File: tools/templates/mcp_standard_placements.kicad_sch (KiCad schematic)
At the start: 150 parts, among them J1 ICSP, J3 PIR BOARD, J5 MOTOR, J6 DNP, Q1 FMOS3401A?, Q11 MMBTA55?, Q2 BC847B?, Q3 MMBTA55?, Q4 MMBTA55?, Q5 MMBTA55?, Q6 MMBTA55?, Q7 BC857C?, Q8 N/P pair? (372A), Q9 DNP, U1 S-1200B45? [pins], U106 U6A / DNP, U2 SN74LVC2G14DBV?, U3 SGM8542XS, U4 PIC16F18855, U5 MX512H, U6 S-812C33AMC? / 3.3V, U7 DNP, Y1 20 MHz

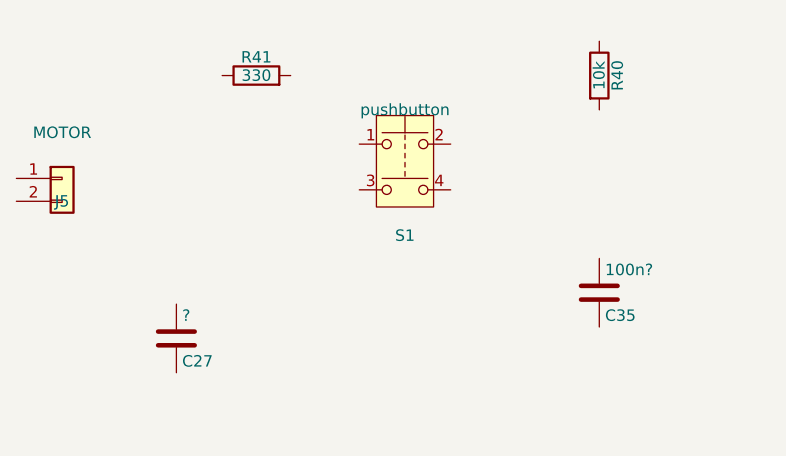
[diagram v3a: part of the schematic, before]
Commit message: Assign stock S1 tactile footprint from measured body dimensions
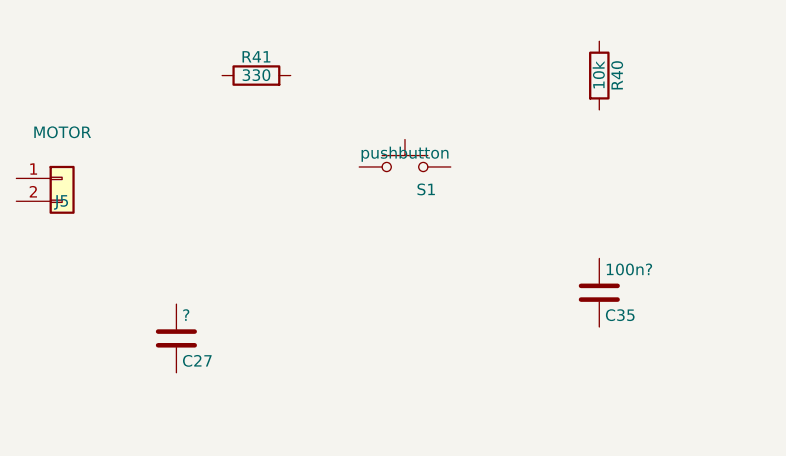
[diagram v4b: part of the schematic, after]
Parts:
- removed S1: pushbutton, symbol Switch:SW_Push_Dual
- added S1: pushbutton, Button_Switch_SMD:SW_SPST_PTS645Sx43SMTR92, symbol Switch:SW_Push
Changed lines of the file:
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@@
 	)
 	(symbol
-		(lib_id "Switch:SW_Push_Dual")
-		(at 537.21 60.96 0)
-		(unit 1)
-		(body_style 1)
-		(exclude_from_sim no)
-		(in_bom yes)
-		(on_board yes)
-		(in_pos_files yes)
-		(dnp no)
-		(property "Reference" "S1"
-			(at 537.21 68.58 0)
-			(show_name no)
-			(do_not_autoplace no)
-			(effects
-				(font
-					(size 1.27 1.27)
-				)
-			)
-		)
-		(property "Value" "pushbutton"
-			(at 537.21 54.61 0)
-			(show_name no)
-			(do_not_autoplace no)
-			(effects
-				(font
-					(size 1.27 1.27)
-				)
-			)
-		)
-		(property "Footprint" ""
-			(at 537.21 68.58 0)
-			(hide yes)
-			(show_name no)
-			(do_not_autoplace no)
-			(effects
-				(font
-					(size 1.27 1.27)
-				)
-			)
-		)
-		(property "Datasheet" ""
-			(at 537.21 60.96 0)
-			(hide yes)
-			(show_name no)
-			(do_not_autoplace no)
-			(effects
-				(font
-					(size 1.27 1.27)
-				)
-			)
-		)
-		(property "Description" "Push button switch, generic, symbol, four pins"
-			(at 537.21 60.96 0)
-			(hide yes)
-			(show_name no)
-			(do_not_autoplace no)
-			(effects
-				(font
-					(size 1.27 1.27)
-				)
-			)
-		)
-		(property "ConnectionEvidence" "v0.9.21 user annotated S1 upper-right to C35 upper/model2 (GND via prior V018); lower-right to C35 lower/model1, R40 lower/model2 and R41 left/model2. User explicitly confirms R41 right/model1 reaches J1 VPP/MCLR. Correct physical-to-native switch mapping TL=1, TR=3, BL=2, BR=4. Top-row/bottom-row common pairs remain a tactile-switch hypothesis; released/pressed behavior has not been measured."
-			(at 537.21 60.96 0)
-			(effects
-				(font
-					(size 1.27 1.27)
-				)
-				(hide yes)
-			)
-		)
-		(pin "1"
-		)
-		(pin "2"
-		)
-		(pin "3"
-		)
-		(pin "4"
-		)
-		(instances
-			(project "PetSafe_1001339"
-				(path "/33a03d59-1679-4e9c-af69-68d086b519af"
-					(reference "S1")
-					(unit 1)
-				)
-			)
-		)
-	)
-	(symbol
 		(lib_id "Device:C")
 		(at 558.8 74.93 0)
@@
 		(at 320.03999999999996 312.42)
 	)
-	(sheet_instances
+	(symbol (lib_id "Switch:SW_Push") (at 537.21 60.96 0) (unit 1)
+(body_style 1) (exclude_from_sim no) (in_bom yes) (on_board yes) (in_pos_files yes) (dnp no)
+(property "Reference" "S1"
+(at 538.48 63.5 0)
+(show_name no)
+(do_not_autoplace no)
+(effects
+				(font
+					(size 1.27 1.27)
+				)
+				(justify left)
+			)
+)
+(property "Value" "pushbutton"
+(at 537.21 59.436 0)
+(show_name no)
+(do_not_autoplace no)
+(effects
+				(font
+					(size 1.27 1.27)
+				)
+			)
+)
+(property "Footprint" "Button_Switch_SMD:SW_SPST_PTS645Sx43SMTR92"
+(at 537.21 66.04 0)
+(hide yes)
+(show_name no)
+(do_not_autoplace no)
+(effects
+				(font
+					(size 1.27 1.27)
+				)
+			)
+)
+(property "Datasheet" "https://www.ckswitches.com/media/1471/pts645.pdf"
+(at 537.21 66.04 0)
+(hide yes)
+(show_name no)
+(do_not_autoplace no)
+(effects
+				(font
+					(size 1.27 1.27)
+				)
+			)
+)
+(property "Description" "Push button switch, generic, symbol, four pins"
+(at 537.21 60.96 0)
+(hide yes)
+(show_name no)
+(do_not_autoplace no)
+(effects
+				(font
+					(size 1.27 1.27)
+				)
+			)
+)
+(property "ConnectionEvidence" "v0.9.23 retains the v0.9.21 button circuit: upper row TL/TR -> GND/C35.2, lower row BL/BR -> H_BUTTON/C35.1/R40.2/R41.2; R41.1 -> J1 VPP. Stock Switch:SW_Push represents the two contact nodes, with physical TL/TR -> native pin1 and BL/BR -> pin2. Four physical pads remain recorded. Common pairs and released/pressed behavior remain inferred from tactile-switch construction, not newly measured." (at 537.21 60.96 0)
+(effects (font (size 1.27 1.27)) (hide yes))
+)
+(property "MechanicalEvidence" "User measured a 6 x 6 x 4 mm body plus 2 mm actuator (about 6 mm overall). Photo shows four SMD gullwing leads; approximate pad-centre span from photo/body ratio is about 8 mm, consistent with the stock PTS645 land pattern (7.96 x 4.50 mm centres). Dimensions select a candidate family, not an exact manufacturer. Library x43 footprint/3D model denotes 4.3 mm overall and must not be used as the measured 6 mm housing." (at 537.21 60.96 0)
+(effects (font (size 1.27 1.27)) (hide yes))
+)
+(property "BodySize" "6 x 6 x 4 mm (user measured)" (at 537.21 60.96 0)
+(effects (font (size 1.27 1.27)) (hide yes))
+)
+(property "ActuatorProtrusion" "2 mm (user measured)" (at 537.21 60.96 0)
+(effects (font (size 1.27 1.27)) (hide yes))
+)
+(property "OverallHeight" "6 mm (4 + 2 mm)" (at 537.21 60.96 0)
+(effects (font (size 1.27 1.27)) (hide yes))
+)
+(property "FootprintStatus" "Candidate 2D land pattern; exact lead span and 6 mm housing variant not verified" (at 537.21 60.96 0)
+(effects (font (size 1.27 1.27)) (hide yes))
+)
+(property "Manufacturer" "Unidentified; PTS645 is a footprint reference" (at 537.21 60.96 0)
+(effects (font (size 1.27 1.27)) (hide yes))
+)
+(property "Model3DStatus" "Stock x43 model is 4.3 mm high; not an exact housing model" (at 537.21 60.96 0)
+(effects (font (size 1.27 1.27)) (hide yes))
+)
+(pin "1")
+(pin "2")
+(instances
+(project "mcp_standard_placements"
+(path "/33a03d59-1679-4e9c-af69-68d086b519af"
+(reference "S1")
+(unit 1)
+)
+)
+)
+)
+(sheet_instances
 		(path "/"
 			(page "1")

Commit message: Group optional circuits by function and replace device placeholders
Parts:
- removed Q9: DNP, Package_TO_SOT_SMD:SOT-23, symbol Connector_Generic:Conn_01x03
- removed TP9: test point, TestPoint:TestPoint_THTPad_D2.0mm_Drill1.0mm, symbol Connector:TestPoint
- removed U106: U6A / DNP, Package_TO_SOT_SMD:SOT-23, symbol Connector_Generic:Conn_01x03
- added Q9: NPN option / DNP, Package_TO_SOT_SMD:SOT-23, symbol Transistor_BJT:Q_NPN_BEC
- added U106: U6A / LDO option, Package_TO_SOT_SMD:SOT-23, symbol Regulator_Linear:MCP1700x-330xxTT
- C49: LocationEvidence (none) -> Clearly visible empty C49 on rear IMG_2442.jpg beside anten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
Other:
- moved on the sheet: C49, D4, D5, D6, J6, R35, R36, TP10, TP104

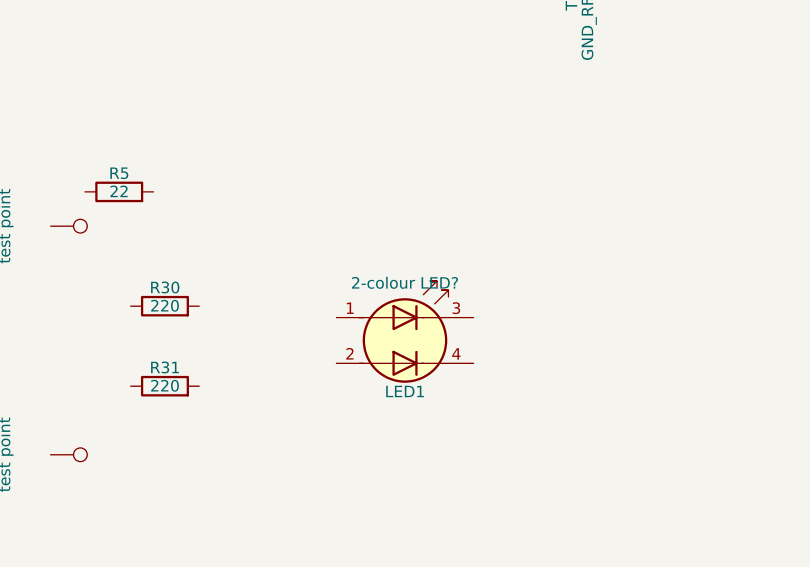
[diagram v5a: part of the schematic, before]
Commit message: Record LED1 red-green emitters and measured square body
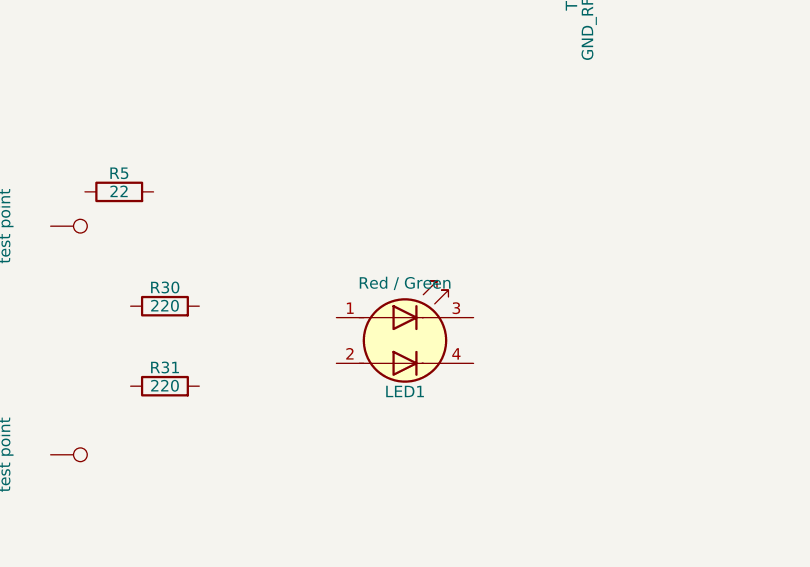
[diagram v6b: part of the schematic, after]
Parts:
- LED1: value 2-colour LED? -> Red / Green; BodySize (none) -> 1.5 x 1.5 mm (user measurement); Colour (none) -> Red / Green; MeasurementEvidence (none) -> User confirms square 1.5 x 1.5 mm package containing red an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
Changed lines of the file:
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@@
 			)
 		)
-		(property "Value" "2-colour LED?"
+		(property "Value" "Red / Green"
 			(at 231.14 231.14 0)
 			(show_name no)
@@
 			)
 		)
+(property "Colour" "Red / Green" (at 231.14 237.49 0)
+(effects (font (size 1.27 1.27)) (hide yes))
+)
+(property "BodySize" "1.5 x 1.5 mm (user measurement)" (at 231.14 237.49 0)
+(effects (font (size 1.27 1.27)) (hide yes))
+)
+(property "MeasurementEvidence" "User confirms square 1.5 x 1.5 mm package containing red and green emitters. Four pads and existing board connections retained. Which resistor/PIC channel lights each colour, internal die pairing and exact manufacturer pad numbering remain unconfirmed. No stock land pattern assigned from body size alone." (at 231.14 237.49 0)
+(effects (font (size 1.27 1.27)) (hide yes))
+)
 		(pin "1"
 		)

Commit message: Assign C5 radial footprint from measured can dimensions
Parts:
- C5: footprint (none) -> Capacitor_THT:CP_Radial_D6.3mm_P2.50mm; BodySize (none) -> 6.33 mm diameter x 16 mm height (user measurement); Height (none) -> 16 mm; LeadPitch (none) -> 2.5 mm (inferred, not measured); MeasurementEvidence (none) -> User confirms radial electrolytic C5, 6.33 mm diameter and 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
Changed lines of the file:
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@@
 			)
 		)
-		(property "Footprint" ""
+		(property "Footprint" "Capacitor_THT:CP_Radial_D6.3mm_P2.50mm"
 			(at 238.455 177.8 0)
 			(hide yes)
@@
 			)
 		)
+(property "BodySize" "6.33 mm diameter x 16 mm height (user measurement)" (at 237.49 181.61 0)
+(effects (font (size 1.27 1.27)) (hide yes))
+)
+(property "Height" "16 mm" (at 237.49 181.61 0)
+(effects (font (size 1.27 1.27)) (hide yes))
+)
+(property "LeadPitch" "2.5 mm (inferred, not measured)" (at 237.49 181.61 0)
+(effects (font (size 1.27 1.27)) (hide yes))
+)
+(property "MeasurementEvidence" "User confirms radial electrolytic C5, 6.33 mm diameter and 16 mm high; earlier sleeve reading 470 uF / 16 V retained. Standard nominal 6.3 mm footprint assigned; 2.5 mm pitch and 0.8 mm drills remain candidate geometry. Stock footprint describes a 7 mm body, so its housing model is not an exact match. Use measured 16 mm for clearance. Polarity and physical nets unchanged." (at 237.49 181.61 0)
+(effects (font (size 1.27 1.27)) (hide yes))
+)
 		(pin "1"
 		)

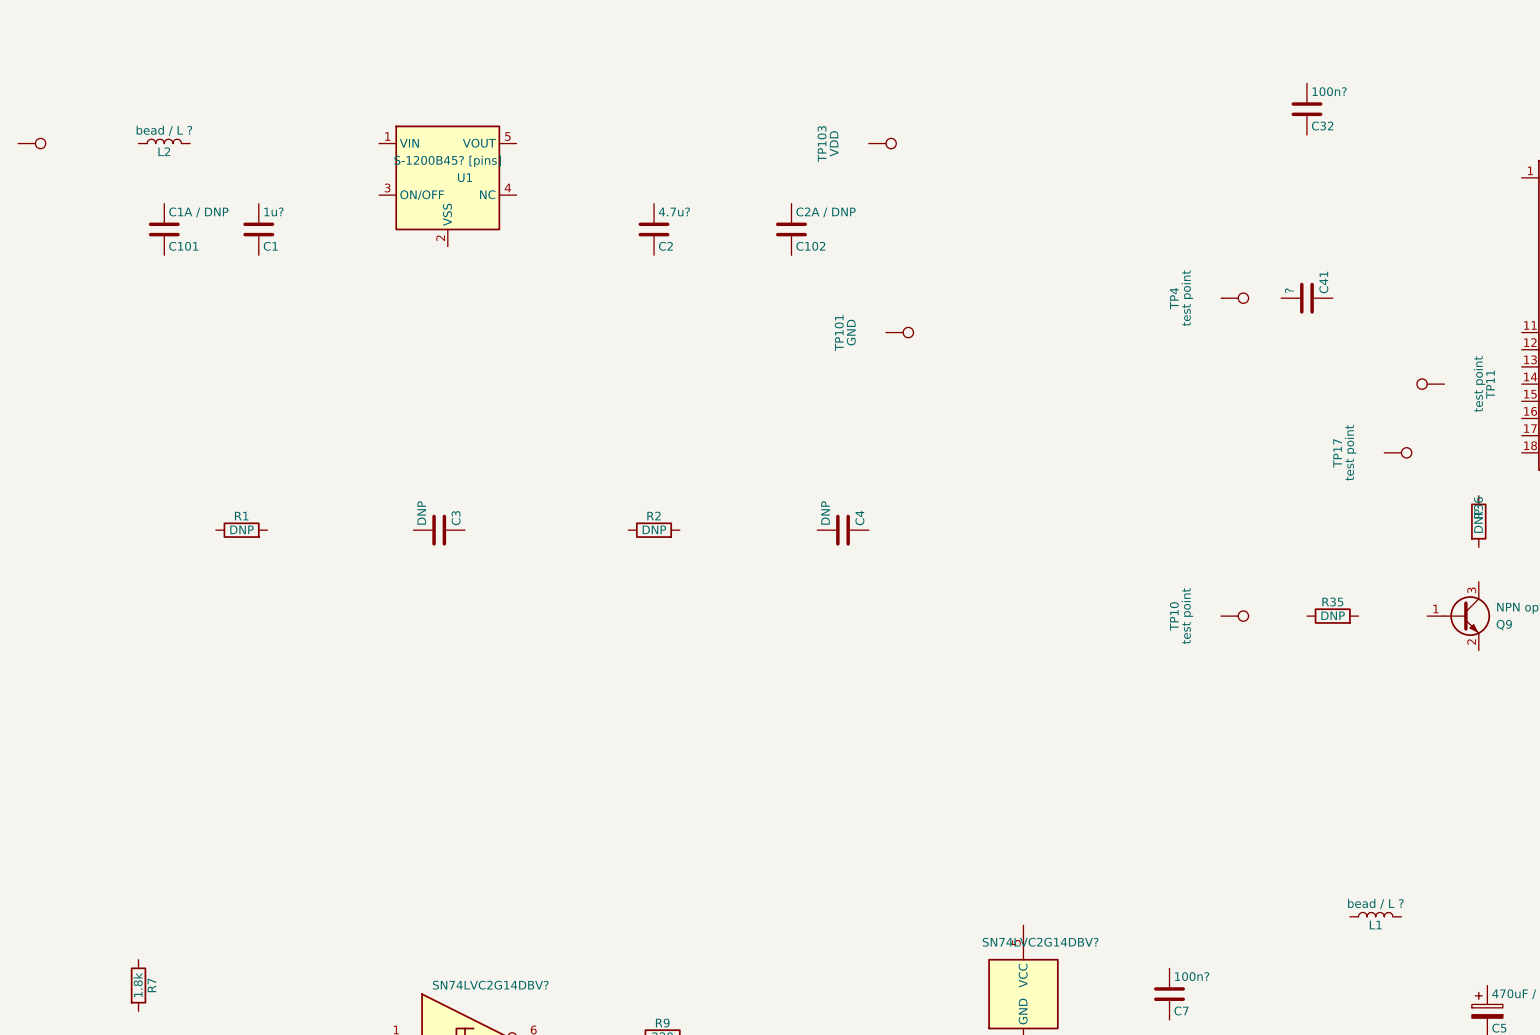
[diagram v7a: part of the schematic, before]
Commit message: Record measured L1 and L2 inductance values
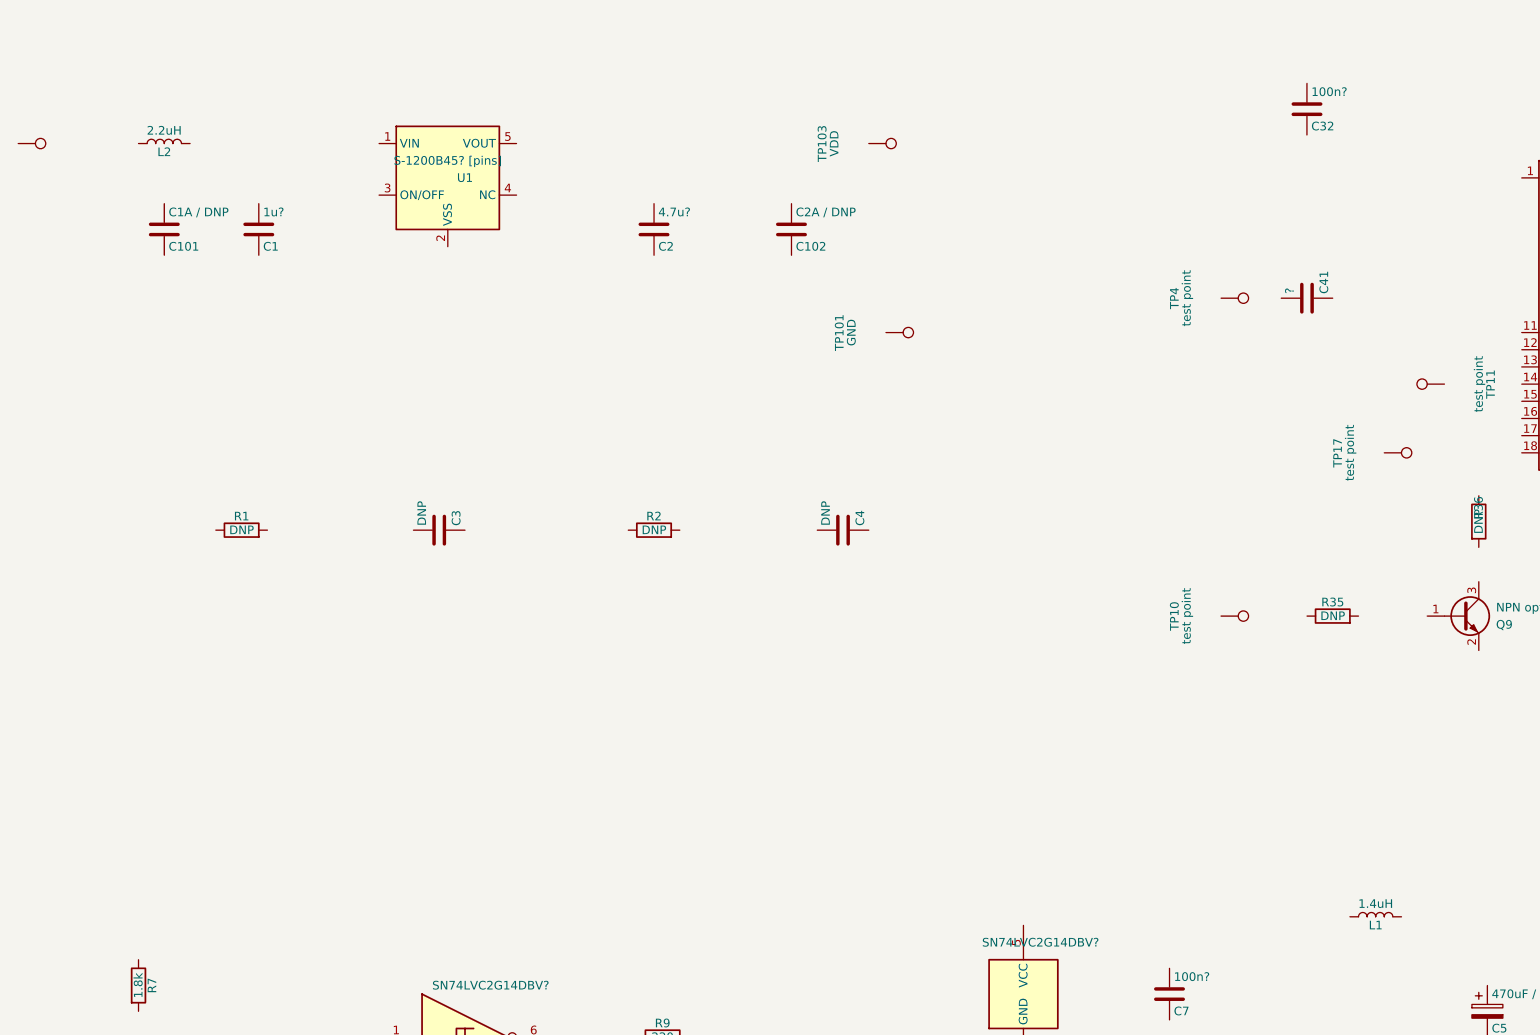
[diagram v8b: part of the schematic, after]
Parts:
- L1: value bead / L ? -> 1.4uH; MeasurementEvidence (none) -> User LCR-meter reading: L1 = 1.4 uH. Test frequency, test m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; ValueSource (none) -> User LCR-meter measurement 2026-10-09
- L2: value bead / L ? -> 2.2uH; MeasurementEvidence (none) -> User LCR-meter reading: L2 = 2.2 uH. Test frequency, test m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; ValueSource (none) -> User LCR-meter measurement 2026-10-09
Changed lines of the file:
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@@
 			)
 		)
-		(property "Value" "bead / L ?"
+		(property "Value" "2.2uH"
 			(at 41.91 51.435 90)
 			(show_name no)
@@
 			)
 		)
+(property "MeasurementEvidence" "User LCR-meter reading: L2 = 2.2 uH. Test frequency, test mode, fixture compensation and in-circuit/isolation condition not yet reported. Recorded reading; manufacturer nominal, tolerance, DCR and current rating remain unknown." (at 41.91 53.34 0)
+(effects (font (size 1.27 1.27)) (hide yes))
+)
+(property "ValueSource" "User LCR-meter measurement 2026-10-09" (at 41.91 53.34 0)
+(effects (font (size 1.27 1.27)) (hide yes))
+)
 		(pin "1"
 		)
@@
 			)
 		)
-		(property "Value" "bead / L ?"
+		(property "Value" "1.4uH"
 			(at 220.98 165.735 90)
 			(show_name no)
@@
 			)
 		)
+(property "MeasurementEvidence" "User LCR-meter reading: L1 = 1.4 uH. Test frequency, test mode, fixture compensation and in-circuit/isolation condition not yet reported. Recorded reading; manufacturer nominal, tolerance, DCR and current rating remain unknown." (at 220.98 167.64 0)
+(effects (font (size 1.27 1.27)) (hide yes))
+)
+(property "ValueSource" "User LCR-meter measurement 2026-10-09" (at 220.98 167.64 0)
+(effects (font (size 1.27 1.27)) (hide yes))
+)
 		(pin "1"
 		)
